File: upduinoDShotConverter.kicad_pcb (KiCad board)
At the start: 2 copper layers, 55 x 70 mm, 11 parts, among them J1 ESC_OUT, J2 5V and Buzzer In, J3 VBAT_and_motors_1-4_in, J5 Motors_5-8_in

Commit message: lots of tweaks, solid design. About to attempt orientation shift
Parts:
- added J4: Conn_01x24_Pin, Connector_PinHeader_2.54mm:PinHeader_1x24_P2.54mm_Vertical, F.Cu at (116.8, 34.0)
- added J6: Conn_01x24_Pin, Connector_PinHeader_2.54mm:PinHeader_1x24_P2.54mm_Vertical, F.Cu at (129.5, 92.4)
- moved R2 29.9 mm to (121.7, 60.0)
- moved R1 29.1 mm to (121.7, 55.8)
- moved J2 5.59 mm to (144.2, 67.4)
- moved J1 2.79 mm to (144.1, 81.0)
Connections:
- U1 pad 11: unconnected-(U1-gpio_23-Pad11) -> Net-(J4-Pin_11)
- U1 pad 12: unconnected-(U1-gpio_25-Pad12) -> Net-(J4-Pin_12)
- U1 pad 16: unconnected-(U1-gpio_35-Pad16) -> Net-(J4-Pin_16)
- U1 pad 18: unconnected-(U1-gpio_37-Pad18) -> Net-(J4-Pin_18)
- U1 pad 2: unconnected-(U1-VIO-Pad2) -> Net-(J4-Pin_2)
- U1 pad 23: unconnected-(U1-gpio_38-Pad23) -> Net-(J4-Pin_23)
- U1 pad 24: unconnected-(U1-gpio_28-Pad24) -> Net-(J4-Pin_24)
- U1 pad 25: unconnected-(U1-gpio_2-Pad25) -> Net-(J6-Pin_1)
- U1 pad 26: Net-(J1-Pin_3) -> Net-(J6-Pin_2)
- U1 pad 27: Net-(J1-Pin_4) -> Net-(J6-Pin_3)
- U1 pad 28: unconnected-(U1-gpio_45-Pad28) -> Net-(J6-Pin_4)
- U1 pad 29: unconnected-(U1-gpio_48-Pad29) -> Net-(J6-Pin_5)
- U1 pad 3: unconnected-(U1-RST-Pad3) -> Net-(J4-Pin_3)
- U1 pad 30: unconnected-(U1-gpio_3-Pad30) -> Net-(J6-Pin_6)
- U1 pad 31: unconnected-(U1-gpio_4-Pad31) -> Net-(J6-Pin_7)
- U1 pad 32: unconnected-(U1-gpio_44-Pad32) -> Net-(J6-Pin_8)
- U1 pad 33: unconnected-(U1-gpio_6-Pad33) -> Net-(J6-Pin_9)
- U1 pad 34: unconnected-(U1-gpio_9-Pad34) -> Net-(J6-Pin_10)
- U1 pad 35: unconnected-(U1-gpio_11-Pad35) -> Net-(J6-Pin_11)
- U1 pad 36: unconnected-(U1-gpio_18-Pad36) -> Net-(J6-Pin_12)
- U1 pad 37: unconnected-(U1-gpio_19-Pad37) -> Net-(J6-Pin_13)
- U1 pad 38: unconnected-(U1-gpio_13-Pad38) -> Net-(J6-Pin_14)
- U1 pad 39: unconnected-(U1-gpio_21-Pad39) -> Net-(J1-Pin_3)
- U1 pad 4: unconnected-(U1-DONE-Pad4) -> Net-(J4-Pin_4)
- U1 pad 40: unconnected-(U1-gpio_12-Pad40) -> Net-(J1-Pin_4)
- U1 pad 41: unconnected-(U1-12Mhz-Pad41) -> Net-(J6-Pin_17)
- U1 pad 43: unconnected-(U1-gpio_10-Pad43) -> Net-(J6-Pin_19)
- U1 pad 44: unconnected-(U1-gpio_20-Pad44) -> Net-(J6-Pin_20)
- U1 pad 45: unconnected-(U1-spi_miso-Pad45) -> Net-(J6-Pin_21)
- U1 pad 46: unconnected-(U1-spi_mosi-Pad46) -> Net-(J6-Pin_22)
- U1 pad 47: unconnected-(U1-spi_sck-Pad47) -> Net-(J6-Pin_23)
- U1 pad 48: unconnected-(U1-spi_ssn-Pad48) -> Net-(J6-Pin_24)
- U1 pad 5: unconnected-(U1-RGB2-Pad5) -> Net-(J4-Pin_5)
- U1 pad 6: unconnected-(U1-RGB0-Pad6) -> Net-(J4-Pin_6)
- U1 pad 7: unconnected-(U1-RGB1-Pad7) -> Net-(J4-Pin_7)
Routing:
- net +3.3V: track 39.6 -> 11.6 mm
- net Net-(J1-Pin_4): track 21.8 -> 40.5 mm, vias 0 -> 1
- net Net-(J1-Pin_3): track 22.4 -> 40.8 mm, vias 0 -> 1
- net +5V: track 32.4 -> 44.1 mm
- net GND: track 0.00 -> 7.62 mm
- net +BATT: track 67.5 -> 61.7 mm
- net Net-(J1-Pin_2): track 21.2 -> 17.6 mm
- net Net-(J3-Pin_4): track 14.6 -> 17.1 mm
- net Net-(J6-Pin_9): track 0.00 -> 2.54 mm
- net Net-(J6-Pin_8): track 0.00 -> 2.54 mm
- net Net-(J6-Pin_7): track 0.00 -> 2.54 mm
- net Net-(J6-Pin_6): track 0.00 -> 2.54 mm
- net Net-(J6-Pin_5): track 0.00 -> 2.54 mm
- net Net-(J6-Pin_4): track 0.00 -> 2.54 mm
- net Net-(J6-Pin_3): track 0.00 -> 2.54 mm
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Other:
- board text added: "Patronics DShot-i2c Converter 1.0 2024"

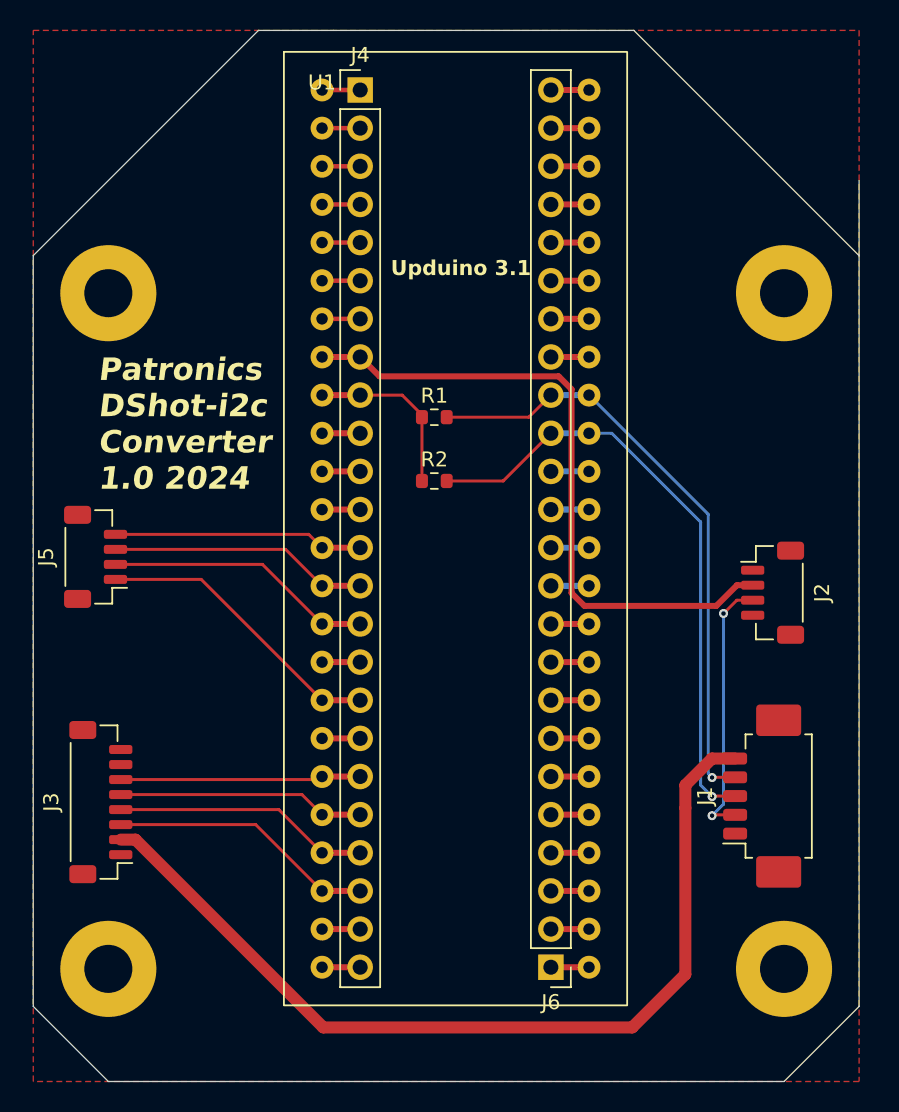
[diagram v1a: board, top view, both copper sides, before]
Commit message: sucessful orientation shift, along with additional GPIO breakouts and via arrows
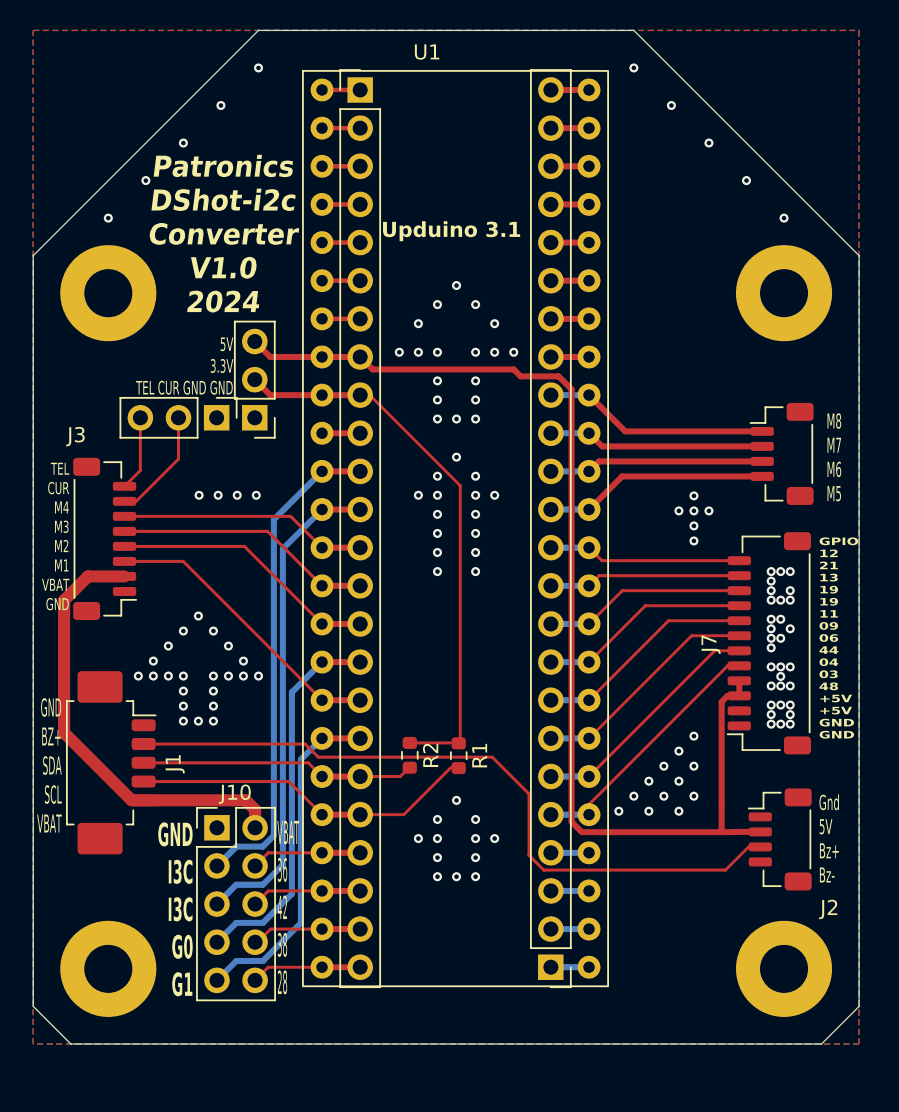
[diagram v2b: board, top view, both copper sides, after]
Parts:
- added J10: Conn_02x05_Odd_Even, Connector_PinHeader_2.54mm:PinHeader_2x05_P2.54mm_Vertical, F.Cu at (107.2, 83.1)
- added J7: Conn_01x12_Socket, Connector_JST:JST_SH_SM12B-SRSS-TB_1x12-1MP_P1.00mm_Horizontal, F.Cu at (144.0, 70.8)
- added J8: Conn_01x03_Pin, Connector_PinHeader_2.54mm:PinHeader_1x03_P2.54mm_Vertical, F.Cu at (109.8, 55.8)
- added J9: Conn_01x02_Pin, Connector_PinHeader_2.54mm:PinHeader_1x03_P2.54mm_Vertical, F.Cu at (107.2, 55.8)
- moved J5 46.2 mm to (144.9, 58.2), turned to -90 degrees
- moved J1 44.2 mm to (100.0, 78.8), turned to -90 degrees
- moved R1 22.6 mm to (123.3, 78.3), turned to -90 degrees
- moved R2 18.3 mm to (120.1, 78.3), turned to -90 degrees
- moved J3 17.5 mm to (99.8, 63.9)
- moved J2 16.4 mm to (144.7, 83.9)
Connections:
- net Net-(J4-Pin_11) renamed I3C1
- net Net-(J4-Pin_12) renamed I3C2
- net Net-(J4-Pin_16) renamed G0
- net Net-(J4-Pin_18) renamed G1
- J3 pad 7: unconnected-(J3-Pin_7-Pad7) -> Net-(J3-Pin_7)
- J3 pad 8: unconnected-(J3-Pin_8-Pad8) -> Net-(J3-Pin_8)
- J4 pad 13: Net-(J4-Pin_13) -> Net-(J3-Pin_6)
- J4 pad 14: Net-(J4-Pin_14) -> Net-(J3-Pin_5)
- J4 pad 15: Net-(J4-Pin_15) -> Net-(J3-Pin_4)
- J4 pad 17: Net-(J4-Pin_17) -> Net-(J3-Pin_3)
- J4 pad 19: Net-(J3-Pin_6) -> Net-(J1-Pin_3)
- J4 pad 20: Net-(J3-Pin_5) -> Net-(J1-Pin_4)
- J4 pad 21: Net-(J3-Pin_4) -> Net-(J10-Pin_4)
- J4 pad 22: Net-(J3-Pin_3) -> Net-(J10-Pin_6)
- J5 pad 1: Net-(J4-Pin_17) -> Net-(J5-Pin_1)
- J5 pad 2: Net-(J4-Pin_15) -> Net-(J5-Pin_2)
- J5 pad 3: Net-(J4-Pin_14) -> Net-(J5-Pin_3)
- J5 pad 4: Net-(J4-Pin_13) -> Net-(J5-Pin_4)
- J6 pad 13: Net-(J6-Pin_13) -> Net-(J5-Pin_4)
- J6 pad 14: Net-(J6-Pin_14) -> Net-(J5-Pin_3)
- J6 pad 15: Net-(J1-Pin_3) -> Net-(J5-Pin_2)
- J6 pad 16: Net-(J1-Pin_4) -> Net-(J5-Pin_1)
- U1 pad 13: Net-(J4-Pin_13) -> Net-(J3-Pin_6)
- U1 pad 14: Net-(J4-Pin_14) -> Net-(J3-Pin_5)
- U1 pad 15: Net-(J4-Pin_15) -> Net-(J3-Pin_4)
- U1 pad 17: Net-(J4-Pin_17) -> Net-(J3-Pin_3)
- U1 pad 19: Net-(J3-Pin_6) -> Net-(J1-Pin_3)
- U1 pad 20: Net-(J3-Pin_5) -> Net-(J1-Pin_4)
- U1 pad 21: Net-(J3-Pin_4) -> Net-(J10-Pin_4)
- U1 pad 22: Net-(J3-Pin_3) -> Net-(J10-Pin_6)
- U1 pad 37: Net-(J6-Pin_13) -> Net-(J5-Pin_4)
- U1 pad 38: Net-(J6-Pin_14) -> Net-(J5-Pin_3)
- U1 pad 39: Net-(J1-Pin_3) -> Net-(J5-Pin_2)
- U1 pad 40: Net-(J1-Pin_4) -> Net-(J5-Pin_1)
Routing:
- net +BATT: track 61.7 -> 29.6 mm
- net +5V: track 44.1 -> 75.9 mm
- net I3C2: track 2.54 -> 32.8 mm
- net I3C1: track 2.54 -> 32.8 mm
- net Net-(J1-Pin_2): track 17.6 -> 47.6 mm, vias 2 -> 0
- net +3.3V: track 11.6 -> 36.5 mm
- net G0: track 2.54 -> 25.1 mm
- net Net-(J1-Pin_3): track 40.8 -> 18.3 mm, vias 1 -> 0
- net G1: track 2.54 -> 22.6 mm
- net Net-(J4-Pin_17): track 19.6 -> 0.00 mm
- net Net-(J4-Pin_15): track 17.9 -> 0.00 mm
- net Net-(J1-Pin_4): track 40.5 -> 22.7 mm, vias 1 -> 0
- net Net-(J4-Pin_14): track 17.3 -> 0.00 mm
- net Net-(J4-Pin_13): track 16.7 -> 0.00 mm
- net Net-(J5-Pin_1): track 0.00 -> 15.1 mm
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- added copper zone on B.Cu, net GND
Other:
- board size 55 x 70 mm -> 55 x 67.5 mm
- board text added: "5V 3.3V TEL CUR GND GND"
- board text added: "GND BZ+ SDA SCL VBAT"
- board text added: "GND I3C I3C G0 G1"
- board text added: "GPIO 12 21 13 19 19 11 09 06 44 04 03 48 +5V +5V GND GND"
- board text added: "Gnd 5V Bz+ Bz-"
- board text added: "M8 M7 M6 M5"
- board text added: "Patronics DShot-i2c Converter V1.0 2024"
- board text added: "TEL CUR M4 M3 M2 M1 VBAT GND"
- board text added: "VBAT 36 42 38 28"
- board text removed: "Patronics DShot-i2c Converter 1.0 2024"

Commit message: finalize design for v1.0 release, and assign parts from LCSC/JLCPCB
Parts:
- J2, J5: footprint Connector_JST:JST_SH_BM04B-SRSS-TB_1x04-1MP_P1.00mm_Vertical -> Connector_JST:JST_SH_SM04B-SRSS-TB_1x04-1MP_P1.00mm_Horizontal
- J3: footprint Connector_JST:JST_SH_BM08B-SRSS-TB_1x08-1MP_P1.00mm_Vertical -> Connector_JST:JST_SH_SM08B-SRSS-TB_1x08-1MP_P1.00mm_Horizontal
- moved J3 1.00 mm to (100.8, 63.9), turned to -90 degrees
- turned J2 to 90 degrees
- turned J5 to 90 degrees
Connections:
- J2 pad 1: GND -> unconnected-(J2-Pin_1-Pad1)
- J2 pad 2: +5V -> Net-(J1-Pin_2)
- J2 pad 3: Net-(J1-Pin_2) -> +5V
- J2 pad 4: unconnected-(J2-Pin_4-Pad4) -> GND
- J3 pad 1: GND -> Net-(J3-Pin_1)
- J3 pad 2: +BATT -> Net-(J3-Pin_2)
- J3 pad 7: Net-(J3-Pin_7) -> +BATT
- J3 pad 8: Net-(J3-Pin_8) -> GND
- J4 pad 13: Net-(J3-Pin_6) -> Net-(J3-Pin_3)
- J4 pad 14: Net-(J3-Pin_5) -> Net-(J3-Pin_4)
- J4 pad 15: Net-(J3-Pin_4) -> Net-(J3-Pin_5)
- J4 pad 17: Net-(J3-Pin_3) -> Net-(J3-Pin_6)
- J6 pad 13: Net-(J5-Pin_4) -> Net-(J5-Pin_1)
- J6 pad 14: Net-(J5-Pin_3) -> Net-(J5-Pin_2)
- J6 pad 15: Net-(J5-Pin_2) -> Net-(J5-Pin_3)
- J6 pad 16: Net-(J5-Pin_1) -> Net-(J5-Pin_4)
- J9 pad 2: Net-(J3-Pin_7) -> Net-(J3-Pin_2)
- J9 pad 3: Net-(J3-Pin_8) -> Net-(J3-Pin_1)
- U1 pad 13: Net-(J3-Pin_6) -> Net-(J3-Pin_3)
- U1 pad 14: Net-(J3-Pin_5) -> Net-(J3-Pin_4)
- U1 pad 15: Net-(J3-Pin_4) -> Net-(J3-Pin_5)
- U1 pad 17: Net-(J3-Pin_3) -> Net-(J3-Pin_6)
- U1 pad 37: Net-(J5-Pin_4) -> Net-(J5-Pin_1)
- U1 pad 38: Net-(J5-Pin_3) -> Net-(J5-Pin_2)
- U1 pad 39: Net-(J5-Pin_2) -> Net-(J5-Pin_3)
- U1 pad 40: Net-(J5-Pin_1) -> Net-(J5-Pin_4)
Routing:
- net Net-(J3-Pin_7): track 7.51 -> 0.00 mm
- net Net-(J3-Pin_2): track 0.00 -> 6.81 mm
- net Net-(J3-Pin_8): track 5.00 -> 0.00 mm
- net Net-(J3-Pin_1): track 0.00 -> 4.82 mm
- net Net-(J3-Pin_3): track 19.5 -> 14.9 mm
- net Net-(J3-Pin_4): track 17.8 -> 15.5 mm
- net +BATT: track 29.6 -> 31.7 mm
- net +5V: track 75.9 -> 74.5 mm
- net Net-(J3-Pin_6): track 16.6 -> 17.8 mm
- net Net-(J3-Pin_5): track 17.2 -> 16.2 mm
- net Net-(J5-Pin_2): track 14.4 -> 13.7 mm
- net Net-(J5-Pin_1): track 15.1 -> 14.3 mm
- net Net-(J1-Pin_2): track 47.6 -> 46.9 mm
- net Net-(J5-Pin_4): track 15.0 -> 14.4 mm
- net Net-(J5-Pin_3): track 14.3 -> 13.8 mm
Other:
- board text added: "GND 5V BUZZER"
- board text added: "MOTORS 1-4 HIGH POWER"
- board text added: "MOTORS 5-8"
- board text added: "OUT TO ESC"
- board text added: "Patrick Leiser"
